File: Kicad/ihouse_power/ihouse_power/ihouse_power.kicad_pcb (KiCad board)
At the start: 2 copper layers, 293 x 110 mm, 162 parts, among them J1 Conn_02x12_Top_Bottom, J10 Conn_02x07_Odd_Even, J11 Conn_01x06, J13 RC, J14 Optic, J15 Hum1, J16 Hum2, J17 Hum3, J18 Temp, J19 I2C, J2 Conn_02x05_Top_Bottom, J20 Conn_02x05_Odd_Even, J21 Conn_02x02_Top_Bottom, J3 Conn_01x20, J4 Conn_01x20, J5 Conn_01x16, J6 Conn_01x06, J7 Conn_02x07_Odd_Even, J8 Conn_01x16, J9 Conn_01x06, K1 FINDER-34.51, K10 FINDER-34.51, K11 FINDER-41.52, K12 FINDER-34.51, K13 FINDER-34.51, K14 FINDER-34.51, K2 FINDER-34.51, K3 FINDER-34.51, K4 FINDER-34.51, K5 FINDER-34.51, K6 FINDER-34.51, K7 FINDER-34.51, K8 FINDER-34.51, K9 FINDER-34.51, M1 stm32f1_module, M2 tb387_uart_expander, SW1 SW_SPST, U1 ULN2004, U10 MAX232, U11 L7805, U12 MCP23017_SO, U13 L293D, U2 ULN2004, U3 L293D, U4 MCP23017_SO, U5 L7805, U6 EL814, U7 EL814, U8 EL814, U9 24LC32

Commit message: programos rasymas, schemos ir pcb koregavimai. veikia stm bootloaderis per Demonstrator
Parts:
- removed C28: CP, Capacitor_THT:CP_Radial_D4.0mm_P2.00mm
- removed C29: C, Capacitor_SMD:C_0805_2012Metric_Pad1.15x1.40mm_HandSolder
- removed J20: Conn_02x05_Odd_Even, Connector_IDC:IDC-Header_2x05_P2.54mm_Vertical
- removed J21: Conn_02x02_Top_Bottom, Connector_Molex:Molex_Mini-Fit_Jr_5566-04A_2x02_P4.20mm_Vertical
- removed the JP at (91.0, 101.3)
- removed the K14 at (216.8, 98.0)
- removed R12, R13, R34: 4.7k, Resistor_SMD:R_0805_2012Metric_Pad1.15x1.40mm_HandSolder
- removed SW1: SW_SPST, Button_Switch_THT:SW_PUSH_6mm
- removed TH3: Thermistor_PTC, Resistor_SMD:R_2816_7142Metric
- removed U12: MCP23017_SO, Package_SO:SOIC-28W_7.5x17.9mm_P1.27mm
- removed U13: L293D, Package_DIP:DIP-16_W7.62mm_LongPads
- added JP: 0R, Resistor_SMD:R_0805_2012Metric_Pad1.15x1.40mm_HandSolder, B.Cu at (106.3, 96.4)
- added JP: 0R, Resistor_SMD:R_0805_2012Metric_Pad1.15x1.40mm_HandSolder, B.Cu at (86.0, 106.5)
- added K13: FINDER-34.51, Relay_THT:Relay_SPDT_Finder_34.51_Vertical, F.Cu at (216.8, 98.0)
- moved J2 0.10 mm to (220.8, 121.1)
- renumbered K12 to K11, K13 to K12, K11 to K14
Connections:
- net /MCP23017 modulis/M2EN renamed /MCP23017 modulis/M23EN
- net /MCP23017 modulis/TBCMD renamed /MCP23017 modulis/~TBCMD
- net /MCU plokste/A11 renamed /MCU plokste/QCH_D3
- net /MCU plokste/A12 renamed /MCU plokste/QCH_D2
- net /MCU plokste/B8 renamed /MCU plokste/QCH_D0
- net /MCU plokste/B9 renamed /MCU plokste/QCH_D1
- net /MCU plokste/M2ENA renamed /MCU plokste/M23ENA
- net /MCU plokste/TBCMD renamed /MCU plokste/~TBCMD
- net /Reliu modulis/M2ENA renamed /Reliu modulis/M23ENA
- J3 pad 14: /MCU plokste/A10 -> /MCU plokste/TBRX
- J3 pad 15: /MCU plokste/A9 -> /MCU plokste/TBTX
- J3 pad 8: /MCU plokste/PWM2 -> /MCU plokste/PWM4
- J3 pad 9: /MCU plokste/PWM1 -> /MCU plokste/PWM3
- J4 pad 13: /MCU plokste/PWM3 -> /MCU plokste/PWM1
- J4 pad 14: /MCU plokste/PWM4 -> /MCU plokste/PWM2
- J4 pad 7: /MCU plokste/TBTX -> /MCU plokste/A2
- J4 pad 8: /MCU plokste/TBRX -> /MCU plokste/A3
- K10 pad 11: Net-(K10-Pad11) -> /230L
- K11 pad 11: Net-(K10-Pad11) -> /230L
- K12 pad 11: Net-(K10-Pad11) -> /230L
- K3 pad 11: Net-(K10-Pad11) -> /230L
- K4 pad 11: Net-(K10-Pad11) -> /230L
- K5 pad 11: Net-(K10-Pad11) -> /230L
- K6 pad 11: Net-(K10-Pad11) -> /230L
- K7 pad 11: Net-(K10-Pad11) -> /230L
- K8 pad 11: Net-(K10-Pad11) -> /230L
- K9 pad 11: Net-(K10-Pad11) -> /230L
- M1 pad 13: /MCU plokste/PWM3 -> /MCU plokste/PWM1
- M1 pad 14: /MCU plokste/PWM4 -> /MCU plokste/PWM2
- M1 pad 28: /MCU plokste/PWM2 -> /MCU plokste/PWM4
- M1 pad 29: /MCU plokste/PWM1 -> /MCU plokste/PWM3
- M1 pad 34: /MCU plokste/A10 -> /MCU plokste/TBRX
- M1 pad 35: /MCU plokste/A9 -> /MCU plokste/TBTX
- M1 pad 7: /MCU plokste/TBTX -> /MCU plokste/A2
- M1 pad 8: /MCU plokste/TBRX -> /MCU plokste/A3
- U10 pad 11: /MCU plokste/A9 -> /MCU plokste/A2
- U10 pad 12: /MCU plokste/A10 -> /MCU plokste/A3
- U3 pad 14: /Reliu modulis/M2A -> Net-(K13-Pad11)
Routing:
- net Net-(K10-Pad11): track 60.0 -> 0.00 mm
- net /MCU plokste/A9: track 58.1 -> 0.00 mm
- net /MCU plokste/A10: track 55.2 -> 0.00 mm
- net Net-(K13-Pad11): track 0.00 -> 37.5 mm
- net /Reliu modulis/M3A: track 0.00 -> 37.1 mm
- net /MCU plokste/A3: track 0.00 -> 36.0 mm
- net /MCU plokste/A2: track 0.00 -> 34.8 mm
- net /Reliu modulis/K14L: track 31.4 -> 0.00 mm
- net /MCU plokste/TBRX: track 64.6 -> 34.4 mm, vias 2 -> 0
- net /MCU plokste/TBTX: track 68.2 -> 39.1 mm, vias 2 -> 0
- net /MCU plokste/~RST: track 32.1 -> 7.99 mm, vias 2 -> 0
- net /230L: track 31.8 -> 54.0 mm
- net /Reliu modulis/M2B: track 32.3 -> 36.5 mm
- net /Reliu modulis/M2A: track 26.2 -> 27.9 mm
- removed copper zone on B.Cu, net /Papildomu IO modulis/COM
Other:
- board size 293 x 110 mm -> 212 x 110 mm

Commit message: schemos, pcb ruosimas
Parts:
- removed the JP at (106.3, 96.4)
- removed the JP at (86.0, 106.5)
- added M3: ev1527receiver_module, ev1527:EV1527_Receiver, F.Cu at (131.0, 107.4)
- added REF**: SolderWirePad_1x01_Drill0.8mm, Connector_Wire:SolderWirePad_1x01_Drill0.8mm, F.Cu at (65.8, 100.5)
- added REF**: SolderWirePad_1x01_Drill0.8mm, Connector_Wire:SolderWirePad_1x01_Drill0.8mm, F.Cu at (71.1, 101.4)
- J11: footprint Connector_PinHeader_2.54mm:PinHeader_1x06_P2.54mm_Vertical -> Connector_Molex:Molex_KK-254_AE-6410-06A_1x06_P2.54mm_Vertical
- moved REF** 12.9 mm to (118.0, 113.2)
- moved D9 9.88 mm to (133.9, 118.3)
- moved D7 7.62 mm to (65.8, 45.9), turned to 270 degrees
- moved D8 7.62 mm to (92.3, 45.9), turned to 270 degrees
- moved D6 7.61 mm to (78.9, 45.9), turned to 270 degrees
- moved C10 6.73 mm to (124.2, 113.0), turned to 90 degrees
- moved REF** 6.24 mm to (91.1, 100.8)
- moved REF** 0.85 mm to (65.8, 107.8)
- turned J11 to 0 degrees
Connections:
- net Net-(J13-Pad4) renamed /MCU plokste/RSRCEN
- C14 pad 1: /MCU plokste/A0 -> /MCU plokste/OPTIC_AI
- C15 pad 1: /MCU plokste/A1 -> /MCU plokste/HUM1_AI
- C16 pad 1: /MCU plokste/A4 -> /MCU plokste/HUM2_AI
- C17 pad 1: /MCU plokste/A5 -> /MCU plokste/HUM3_AI
- C21 pad 1: /MCU plokste/A6 -> /MCU plokste/TEMP_AI
- J10 pad 13: /MCP23017 modulis/TBRX -> /MCP23017 modulis/TBTX
- J10 pad 14: /MCP23017 modulis/TBTX -> /MCP23017 modulis/TBRX
- J3 pad 14: /MCU plokste/TBRX -> /MCU plokste/TBTX
- J3 pad 15: /MCU plokste/TBTX -> /MCU plokste/TBRX
- J7 pad 13: /MCU plokste/TBRX -> /MCU plokste/TBTX
- J7 pad 14: /MCU plokste/TBTX -> /MCU plokste/TBRX
- M1 pad 10: /MCU plokste/A5 -> /MCU plokste/HUM3_AI
- M1 pad 11: /MCU plokste/A6 -> /MCU plokste/TEMP_AI
- M1 pad 34: /MCU plokste/TBRX -> /MCU plokste/TBTX
- M1 pad 35: /MCU plokste/TBTX -> /MCU plokste/TBRX
- M1 pad 5: /MCU plokste/A0 -> /MCU plokste/OPTIC_AI
- M1 pad 6: /MCU plokste/A1 -> /MCU plokste/HUM1_AI
- M1 pad 7: /MCU plokste/A2 -> /MCU plokste/NEXRX
- M1 pad 8: /MCU plokste/A3 -> /MCU plokste/NEXTX
- M1 pad 9: /MCU plokste/A4 -> /MCU plokste/HUM2_AI
- R23 pad 1: /MCU plokste/A0 -> /MCU plokste/OPTIC_AI
- R24 pad 1: /MCU plokste/A1 -> /MCU plokste/HUM1_AI
- R25 pad 1: /MCU plokste/A4 -> /MCU plokste/HUM2_AI
- R26 pad 1: /MCU plokste/A5 -> /MCU plokste/HUM3_AI
- R27 pad 1: /MCU plokste/A0 -> /MCU plokste/OPTIC_AI
- R28 pad 1: /MCU plokste/A1 -> /MCU plokste/HUM1_AI
- R29 pad 1: /MCU plokste/A4 -> /MCU plokste/HUM2_AI
- R30 pad 1: /MCU plokste/A5 -> /MCU plokste/HUM3_AI
- R32 pad 1: /MCU plokste/A6 -> /MCU plokste/TEMP_AI
- R33 pad 1: /MCU plokste/A6 -> /MCU plokste/TEMP_AI
- U10 pad 11: /MCU plokste/A2 -> /MCU plokste/NEXRX
- U10 pad 12: /MCU plokste/A3 -> /MCU plokste/NEXTX
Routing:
- net /MCU plokste/QCH_D1: track 8.00 -> 76.3 mm, vias 0 -> 2
- net /MCU plokste/QCH_D0: track 8.23 -> 73.3 mm, vias 0 -> 2
- net /MCU plokste/3VDC: track 41.2 -> 92.3 mm, vias 0 -> 2
- net /MCU plokste/NEXTX: track 0.00 -> 46.3 mm
- net /MCU plokste/QCH_D2: track 8.00 -> 51.5 mm
- net /MCU plokste/QCH_D3: track 8.00 -> 47.7 mm
- net /MCU plokste/A3: track 36.0 -> 0.00 mm
- net /MCU plokste/A6: track 35.7 -> 0.00 mm
- net /MCU plokste/TEMP_AI: track 0.00 -> 35.5 mm
- net /MCU plokste/A2: track 34.8 -> 0.00 mm
- net /MCU plokste/NEXRX: track 0.00 -> 33.6 mm
- net /MCU plokste/OPTIC_AI: track 0.00 -> 27.5 mm
- net /MCU plokste/A0: track 27.5 -> 0.00 mm
- net /MCU plokste/HUM3_AI: track 0.00 -> 25.3 mm
- net /MCU plokste/A5: track 25.3 -> 0.00 mm
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
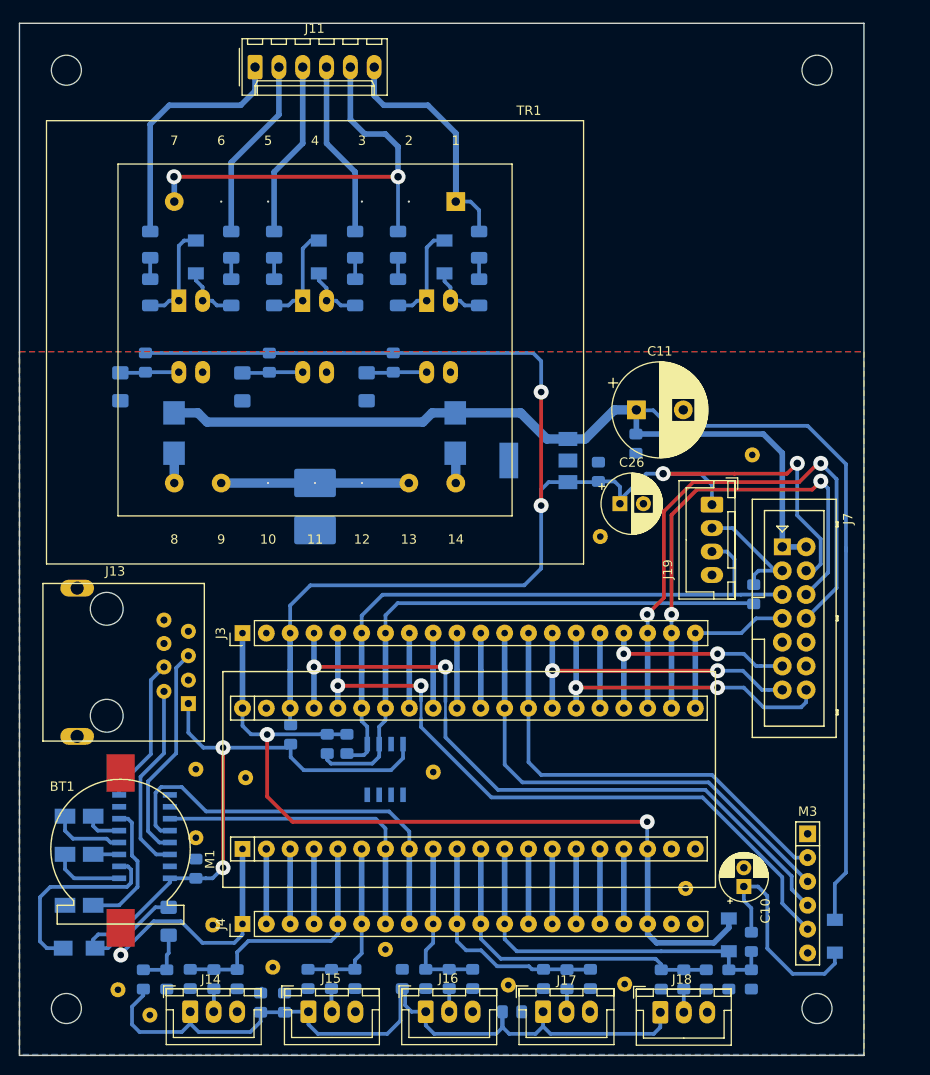
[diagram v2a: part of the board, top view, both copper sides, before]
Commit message: schemos ir pcb plokstes ruosimas
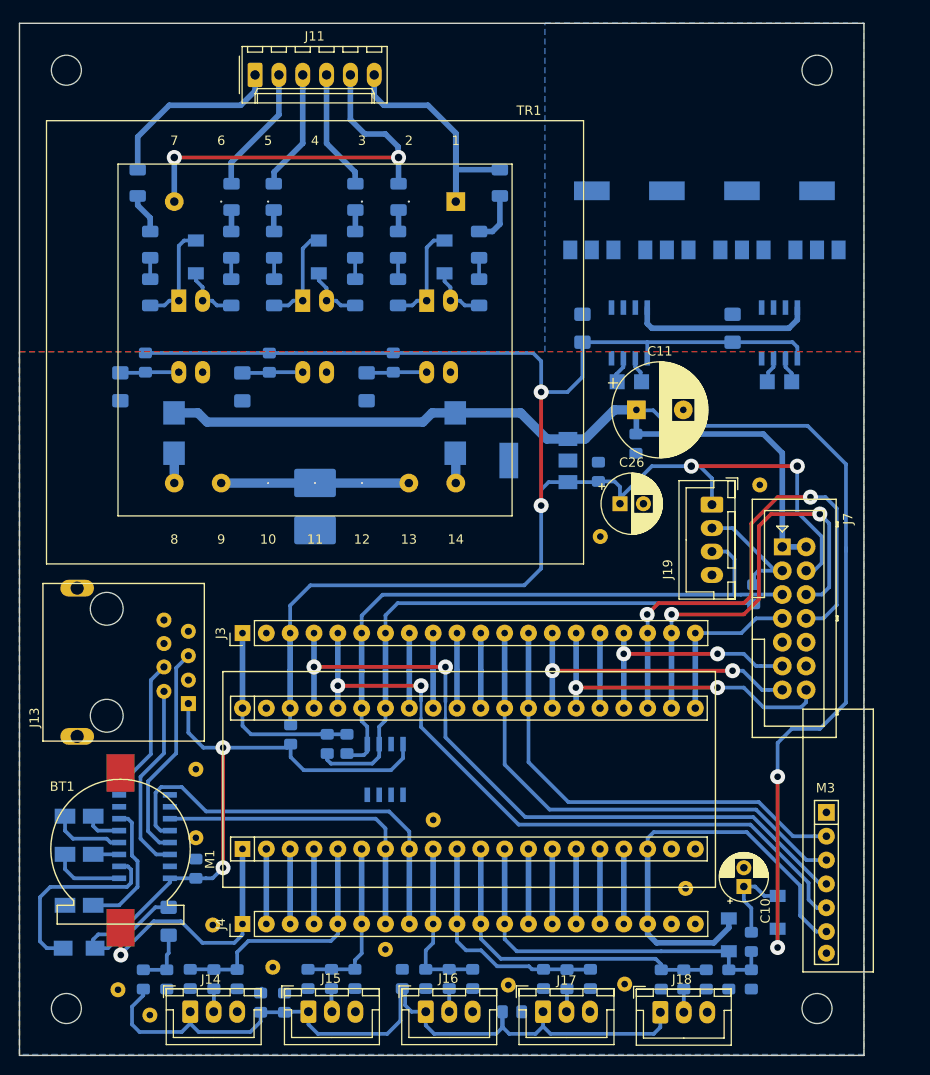
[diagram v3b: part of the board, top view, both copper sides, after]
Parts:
- removed the REF** at (71.1, 101.4)
- added C28: C, Capacitor_SMD:C_1206_3216Metric_Pad1.42x1.75mm_HandSolder, B.Cu at (107.0, 53.5)
- added C29: C, Capacitor_SMD:C_1206_3216Metric_Pad1.42x1.75mm_HandSolder, B.Cu at (123.0, 53.5)
- added R12: 47k, Resistor_SMD:R_1206_3216Metric, B.Cu at (74.1, 39.5)
- added R13: 47k, Resistor_SMD:R_1206_3216Metric, B.Cu at (82.8, 39.5)
- added R34: 47k, Resistor_SMD:R_1206_3216Metric, B.Cu at (59.6, 38.0)
- added R35: 47k, Resistor_SMD:R_1206_3216Metric, B.Cu at (69.6, 39.5)
- added R36: 47k, Resistor_SMD:R_1206_3216Metric, B.Cu at (87.4, 39.5)
- added R37: 47k, Resistor_SMD:R_1206_3216Metric, B.Cu at (98.2, 38.0)
- added REF**: SolderWirePad_1x01_Drill0.8mm, Connector_Wire:SolderWirePad_1x01_Drill0.8mm, F.Cu at (129.3, 59.2)
- added REF**: SolderWirePad_1x01_Drill0.8mm, Connector_Wire:SolderWirePad_1x01_Drill0.8mm, F.Cu at (126.7, 59.2)
- added REF**: SolderWirePad_1x01_Drill0.8mm, Connector_Wire:SolderWirePad_1x01_Drill0.8mm, F.Cu at (113.3, 59.2)
- added REF**: SolderWirePad_1x01_Drill0.8mm, Connector_Wire:SolderWirePad_1x01_Drill0.8mm, F.Cu at (110.7, 59.2)
- added REF**: SOT-223, Package_TO_SOT_SMD:SOT-223, B.Cu at (132.0, 42.0)
- added REF**: SOT-223, Package_TO_SOT_SMD:SOT-223, B.Cu at (124.0, 42.0)
- added REF**: SOT-223, Package_TO_SOT_SMD:SOT-223, B.Cu at (116.0, 42.0)
- added REF**: SOT-223, Package_TO_SOT_SMD:SOT-223, B.Cu at (108.0, 42.0)
- added U12: IR2101, Package_SO:SOIC-8_3.9x4.9mm_P1.27mm, B.Cu at (128.0, 54.0)
- added U13: IR2101, Package_SO:SOIC-8_3.9x4.9mm_P1.27mm, B.Cu at (112.0, 54.0)
- J13: value RC -> RJ33_Shielded
- moved D9 6.61 mm to (127.8, 115.8), turned to 270 degrees
- moved REF** 5.10 mm to (91.1, 105.9)
- moved REF** 3.30 mm to (125.9, 70.2)
- moved M3 3.03 mm to (133.0, 105.1)
- moved J11 0.83 mm to (72.1, 26.5)
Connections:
- M3 pad 6: /MCU plokste/VDDA -> /MCU plokste/3VDC
- R17 pad 1: /MCU plokste/K1.14 -> Net-(R12-Pad2)
- R18 pad 1: /MCU plokste/K1.11 -> Net-(R13-Pad2)
- R19 pad 1: /MCU plokste/K2.14 -> Net-(R19-Pad1)
- R20 pad 1: /MCU plokste/K2.11 -> Net-(R20-Pad1)
- R21 pad 1: /MCU plokste/230N -> Net-(R21-Pad1)
- R22 pad 1: /MCU plokste/230L -> Net-(R22-Pad1)
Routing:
- net /MCU plokste/5VDC: track 233.1 -> 265.1 mm
- net /MCU plokste/3VDC: track 92.3 -> 68.0 mm, vias 2 -> 0
- net /MCU plokste/VB: track 0.00 -> 19.6 mm
- net Net-(C10-Pad1): track 23.7 -> 9.26 mm
- net /MCU plokste/12VDC: track 158.1 -> 167.3 mm, vias 0 -> 2
- net /MCU plokste/K2.14: track 26.6 -> 19.7 mm
- net /MCU plokste/K1.11: track 18.8 -> 12.9 mm
- net /MCU plokste/K2.11: track 19.6 -> 13.7 mm
- net /MCU plokste/K1.14: track 18.8 -> 12.9 mm
- net /MCU plokste/M1ENA: track 51.4 -> 45.8 mm
- net Net-(R22-Pad1): track 0.00 -> 5.54 mm
- net /MCU plokste/M23ENA: track 59.1 -> 54.5 mm
- net Net-(R19-Pad1): track 0.00 -> 4.34 mm
- net /MCU plokste/230N: track 47.4 -> 43.7 mm
- net /MCU plokste/PWM4: track 8.00 -> 10.8 mm
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
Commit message: schemos ir pcb ruosimas
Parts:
- removed the REF** at (65.8, 107.8)
- removed the REF** at (74.0, 121.6)
- removed the REF** at (118.0, 113.2)
- removed the REF** at (60.9, 126.7)
- removed the REF** at (111.5, 123.4)
- removed the REF** at (99.1, 123.5)
- removed the REF** at (86.0, 119.7)
- removed the REF** at (132.0, 42.0)
- removed the REF** at (124.0, 42.0)
- removed the REF** at (116.0, 42.0)
- removed the REF** at (108.0, 42.0)
- removed U12, U13: IR2101, Package_SO:SOIC-8_3.9x4.9mm_P1.27mm
- added ?: BU+, Connector_Wire:SolderWirePad_1x01_Drill0.8mm, B.Cu at (91.4, 98.2)
- added ?: BU-, Connector_Wire:SolderWirePad_1x01_Drill0.8mm, B.Cu at (93.7, 103.5)
- added ?: BUIN, Connector_Wire:SolderWirePad_1x01_Drill0.8mm, B.Cu at (103.8, 105.7)
- added C30: CP, Capacitor_THT:CP_Radial_D8.0mm_P3.50mm, F.Cu at (101.1, 24.0)
- added D11: GBU6A, Diode_THT:Diode_Bridge_Vishay_GBU, F.Cu at (134.0, 39.0)
- added D12: BAS32, Diode_SMD:D_MiniMELF, B.Cu at (96.4, 100.0)
- added F3: 33V/3A, Resistor_THT:R_Axial_DIN0204_L3.6mm_D1.6mm_P5.08mm_Horizontal, B.Cu at (125.0, 42.0)
- added F4: 33V/3A, Resistor_THT:R_Axial_DIN0204_L3.6mm_D1.6mm_P5.08mm_Horizontal, B.Cu at (119.4, 41.9)
- added F5: 33V/3A, Resistor_THT:R_Axial_DIN0204_L3.6mm_D1.6mm_P5.08mm_Horizontal, B.Cu at (114.3, 42.0)
- added F6: 33V/3A, Resistor_THT:R_Axial_DIN0204_L3.6mm_D1.6mm_P5.08mm_Horizontal, B.Cu at (109.0, 42.0)
- added J20: Conn_02x05_Top_Bottom, Connector_Molex:Molex_Mini-Fit_Jr_5566-10A_2x05_P4.20mm_Vertical, F.Cu at (126.9, 38.0)
- added Q1: IRF7403, Package_SO:SOIC-8_3.9x4.9mm_P1.27mm, B.Cu at (126.8, 52.1)
- added Q2: IRF7403, Package_SO:SOIC-8_3.9x4.9mm_P1.27mm, B.Cu at (120.4, 52.1)
- added Q3: IRF7403, Package_SO:SOIC-8_3.9x4.9mm_P1.27mm, B.Cu at (113.8, 52.1)
- added Q4: IRF7403, Package_SO:SOIC-8_3.9x4.9mm_P1.27mm, B.Cu at (107.4, 52.1)
- added Q5: BC847, Package_TO_SOT_SMD:SOT-23, B.Cu at (97.9, 104.6)
- added R38: 100, Resistor_SMD:R_0805_2012Metric_Pad1.15x1.40mm_HandSolder, B.Cu at (124.9, 58.5)
- added R39: 100, Resistor_SMD:R_0805_2012Metric_Pad1.15x1.40mm_HandSolder, B.Cu at (122.2, 58.5)
- added R40: 100, Resistor_SMD:R_0805_2012Metric_Pad1.15x1.40mm_HandSolder, B.Cu at (111.9, 58.5)
- added R41: 100, Resistor_SMD:R_0805_2012Metric_Pad1.15x1.40mm_HandSolder, B.Cu at (109.2, 58.5)
- added R42: 10k, Resistor_SMD:R_0805_2012Metric_Pad1.15x1.40mm_HandSolder, B.Cu at (127.2, 58.5)
- added R43: 10k, Resistor_SMD:R_0805_2012Metric_Pad1.15x1.40mm_HandSolder, B.Cu at (119.9, 58.5)
- added R44: 10k, Resistor_SMD:R_0805_2012Metric_Pad1.15x1.40mm_HandSolder, B.Cu at (114.2, 58.5)
- added R45: 10k, Resistor_SMD:R_0805_2012Metric_Pad1.15x1.40mm_HandSolder, B.Cu at (106.9, 58.5)
- added R46: 10k, Resistor_SMD:R_0805_2012Metric_Pad1.15x1.40mm_HandSolder, B.Cu at (101.0, 104.7)
- added R47: 10k, Resistor_SMD:R_0805_2012Metric_Pad1.15x1.40mm_HandSolder, B.Cu at (98.9, 100.7)
- added R48: 47, Resistor_SMD:R_1206_3216Metric, B.Cu at (93.7, 99.6)
- added REF**: SolderWirePad_1x01_Drill0.8mm, Connector_Wire:SolderWirePad_1x01_Drill0.8mm, F.Cu at (53.0, 101.0)
- added REF**: SolderWirePad_1x01_Drill0.8mm, Connector_Wire:SolderWirePad_1x01_Drill0.8mm, F.Cu at (66.0, 108.0)
- added REF**: SolderWirePad_1x01_Drill0.8mm, Connector_Wire:SolderWirePad_1x01_Drill0.8mm, F.Cu at (66.0, 77.0)
- added REF**: SolderWirePad_1x01_Drill0.8mm, Connector_Wire:SolderWirePad_1x01_Drill0.8mm, F.Cu at (92.0, 77.0)
- added REF**: SolderWirePad_1x01_Drill0.8mm, Connector_Wire:SolderWirePad_1x01_Drill0.8mm, F.Cu at (124.0, 71.0)
- added REF**: SolderWirePad_1x01_Drill0.8mm, Connector_Wire:SolderWirePad_1x01_Drill0.8mm, F.Cu at (133.0, 60.0)
- added REF**: SolderWirePad_1x01_Drill0.8mm, Connector_Wire:SolderWirePad_1x01_Drill0.8mm, F.Cu at (105.0, 62.0)
- C28, C29: value C -> CP; footprint Capacitor_SMD:C_1206_3216Metric_Pad1.42x1.75mm_HandSolder -> Capacitor_THT:CP_Radial_D8.0mm_P3.50mm; moved to F.Cu
- REF**: value SolderWirePad_1x01_Drill0.8mm -> PWM3
- REF**: value SolderWirePad_1x01_Drill0.8mm -> PWM4
- REF**: value SolderWirePad_1x01_Drill0.8mm -> PWM1
- REF**: value SolderWirePad_1x01_Drill0.8mm -> PWM2
- moved C29 42.8 mm to (92.0, 24.0), turned to 270 degrees
- moved C28 38.0 mm to (83.0, 24.0), turned to 270 degrees
- moved REF** 14.3 mm to (111.8, 67.8)
- moved C23 13.4 mm to (126.0, 67.3)
- moved J11 10.2 mm to (61.9, 26.5)
- moved D9 9.06 mm to (119.7, 111.7), turned to 180 degrees
- moved REF** 5.24 mm to (124.7, 61.7)
- moved REF** 5.24 mm to (122.1, 61.7)
- moved C11 5.09 mm to (117.0, 65.0), turned to 90 degrees
- moved REF** 2.97 mm to (109.1, 61.7)
- moved REF** 2.97 mm to (111.7, 61.7)
- moved C3 1.51 mm to (69.2, 59.6)
- moved R2 1.51 mm to (85.3, 57.0)
- moved R3 1.51 mm to (58.9, 57.0)
- moved R4 1.51 mm to (72.1, 57.0)
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- renumbered REF** to 0R, JP to 0R
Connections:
- C28 pad 1: /MCU plokste/5VDC -> /MCU plokste/VB
- C29 pad 1: /MCU plokste/5VDC -> /MCU plokste/VB
- J4 pad 1: /MCU plokste/VBAT -> Net-(J4-Pad1)
- J4 pad 17: /MCU plokste/~RST -> Net-(J4-Pad17)
- J4 pad 20: /MCU plokste/COM1 -> /MCU plokste/12VDC
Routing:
- net /MCU plokste/5VDC: track 265.1 -> 231.2 mm
- net /MCU plokste/12VDC: track 167.3 -> 192.1 mm, vias 2 -> 4
- net /MCU plokste/VB: track 19.6 -> 0.00 mm
- net Net-(D11-Pad2): track 0.00 -> 15.4 mm
- net Net-(D11-Pad3): track 0.00 -> 14.7 mm
- net /MCU plokste/230N: track 43.7 -> 55.2 mm
- net /MCU plokste/K2.14: track 19.7 -> 11.3 mm
- net /MCU plokste/~RST: track 7.99 -> 0.00 mm
- net /MCU plokste/K1.11: track 12.9 -> 19.9 mm
- net /MCU plokste/BUZMN: track 0.00 -> 6.76 mm
- net Net-(Q4-Pad4): track 0.00 -> 6.00 mm
- net Net-(Q2-Pad4): track 0.00 -> 6.00 mm
- net Net-(F3-Pad1): track 0.00 -> 5.35 mm
- net /MCU plokste/VBAT: track 27.9 -> 22.8 mm
- net /MCU plokste/BUZPL: track 0.00 -> 5.00 mm
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- added copper zone on B.Cu, net /MCU plokste/VB
- added copper zone on B.Cu, net Net-(F3-Pad2)
- added copper zone on B.Cu, net Net-(F4-Pad2)
- added copper zone on B.Cu, net Net-(F5-Pad2)
- added copper zone on B.Cu, net Net-(F6-Pad2)

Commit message: schemos ir pcb paruosimas
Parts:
- added REF**: SolderWirePad_1x01_Drill0.8mm, Connector_Wire:SolderWirePad_1x01_Drill0.8mm, F.Cu at (123.0, 108.0)
- added REF**: SolderWirePad_1x01_Drill0.8mm, Connector_Wire:SolderWirePad_1x01_Drill0.8mm, F.Cu at (87.3, 119.5)
- F3, F4, F5, F6: moved to F.Cu
- moved C27 10.9 mm to (111.9, 120.7)
- moved M3 4.03 mm to (132.0, 109.0)
- moved REF** 4.00 mm to (128.0, 126.0)
- moved R11 2.90 mm to (127.0, 120.8)
- moved R37 2.72 mm to (94.8, 39.4)
- moved R10 0.20 mm to (125.0, 118.7)
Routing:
- net /MCU plokste/3VDC: track 69.1 -> 52.4 mm
- net /MCU plokste/QCH_D1: track 76.2 -> 80.5 mm
- net /MCU plokste/QCH_D2: track 49.5 -> 53.7 mm
- net /MCU plokste/QCH_D0: track 74.0 -> 78.2 mm
- net Net-(R22-Pad1): track 5.54 -> 2.20 mm
- net /MCU plokste/QCH_D3: track 46.7 -> 50.0 mm
- net /MCU plokste/SCK: track 75.4 -> 77.8 mm
- net /MCU plokste/230L: track 31.5 -> 29.3 mm
- net /MCU plokste/A7: track 40.4 -> 42.1 mm
- net /MCU plokste/PWM3: track 10.3 -> 10.9 mm

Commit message: schemos ir pcb ruosimas
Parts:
- added ?: LPULSE, Connector_Wire:SolderWirePad_1x01_Drill0.8mm, B.Cu at (85.4, 60.1)
- added ?: LPULSE1, Connector_Wire:SolderWirePad_1x01_Drill0.8mm, B.Cu at (72.1, 60.1)
- added ?: LPULSE2, Connector_Wire:SolderWirePad_1x01_Drill0.8mm, B.Cu at (58.9, 60.1)
- R12, R13, R14, R15, R16, R17, R18, R19, R20, R21, R22, R34, R35, R36, R37, R5, R6, R7: value 47k -> 22k
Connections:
- J3 pad 10: /MCU plokste/B3 -> /MCU plokste/LPULSE
- J4 pad 15: /MCU plokste/B10 -> /MCU plokste/LPULSE1
- J4 pad 16: /MCU plokste/B11 -> /MCU plokste/LPULSE2
- M1 pad 15: /MCU plokste/B10 -> /MCU plokste/LPULSE1
- M1 pad 16: /MCU plokste/B11 -> /MCU plokste/LPULSE2
- M1 pad 30: /MCU plokste/B3 -> /MCU plokste/LPULSE
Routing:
- net /MCU plokste/LPULSE: track 6.55 -> 17.1 mm
- net /MCU plokste/LPULSE2: track 6.80 -> 16.8 mm
- net /MCU plokste/LPULSE1: track 6.81 -> 16.8 mm
- net /MCU plokste/B3: track 8.47 -> 0.00 mm
- net /MCU plokste/B11: track 7.99 -> 0.00 mm
- net /MCU plokste/B10: track 7.99 -> 0.00 mm
